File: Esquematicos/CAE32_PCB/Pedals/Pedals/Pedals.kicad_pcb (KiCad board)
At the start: 4 copper layers, 45 x 55 mm, 64 parts, among them J1 PGRM and SPI, J10 Conn_01x03_Female, J11 Conn_01x03_Female, J12 Conn_01x03_Female, J13 Conn_01x03_Female, J14 USB_C_Receptacle, J15 UART_PGR, J16 ST-Link, J2 Conn_01x07_Female, J3 Conn_01x03_Female, J4 Conn_01x03_Female, J5 Conn_01x03_Female, J6 Conn_01x03_Female, J7 Conn_01x03_Female, J8 Conn_01x03_Female, J9 Conn_01x03_Female, Q1 MMBT3906, SW1 BOOT, SW2 MODE, SW3 RST, U1 STM32F072RBTx, U2 REF3033, U3 ADC128S102, U4 HX711, U5 LDL1117

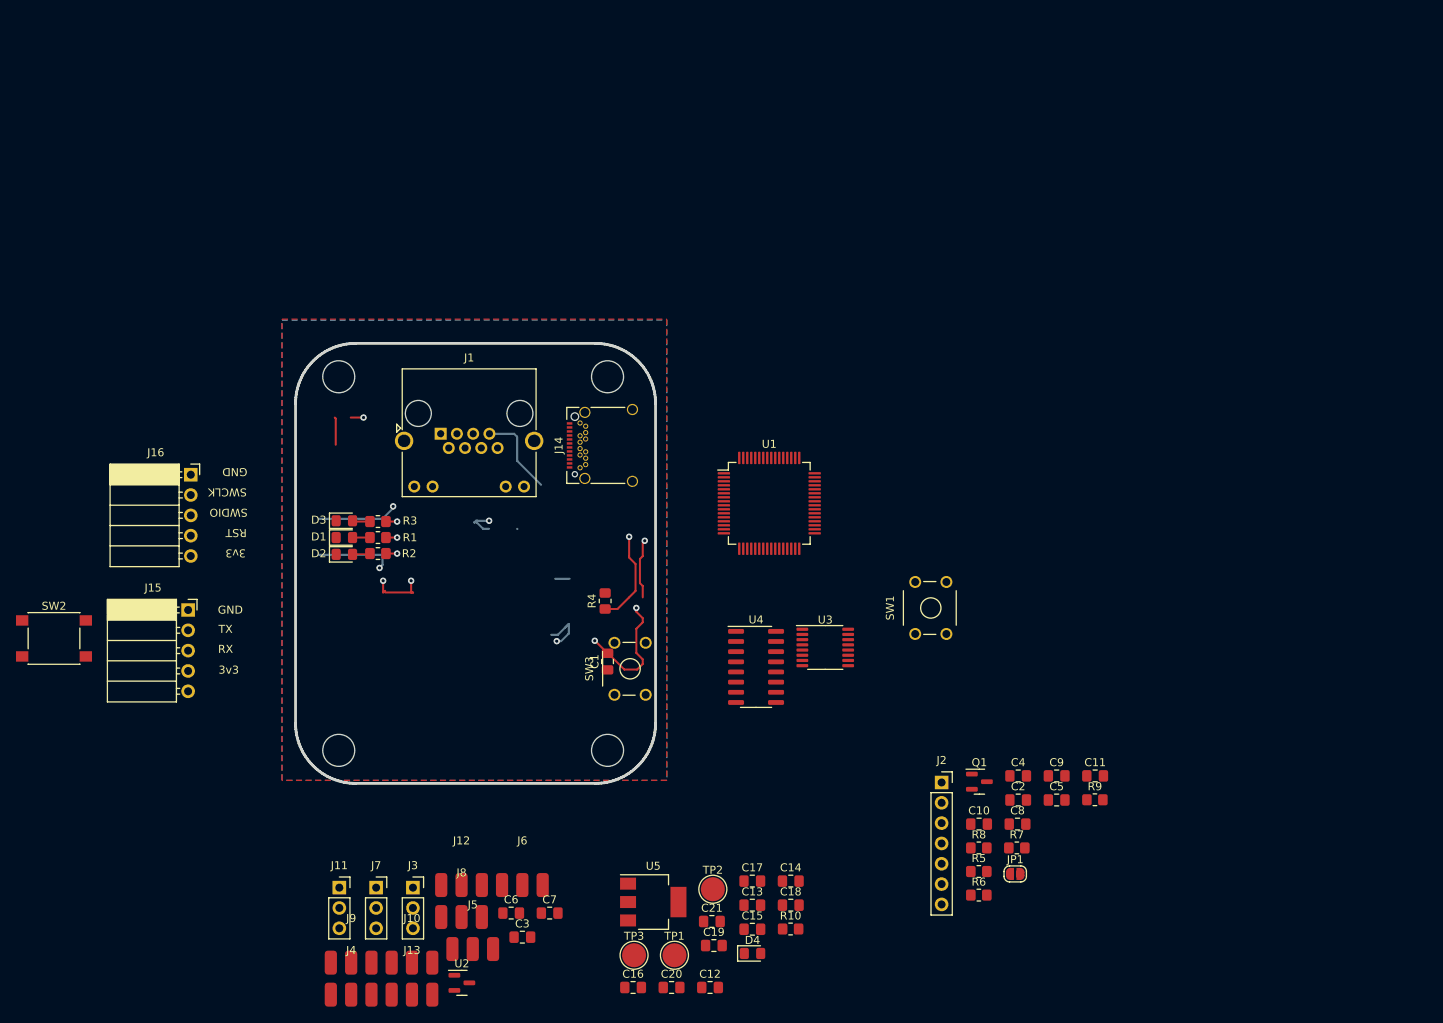
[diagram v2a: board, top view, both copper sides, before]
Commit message: update: se añade otra hoja para las celdas de carga, ademas de reorganizar todas las hojas
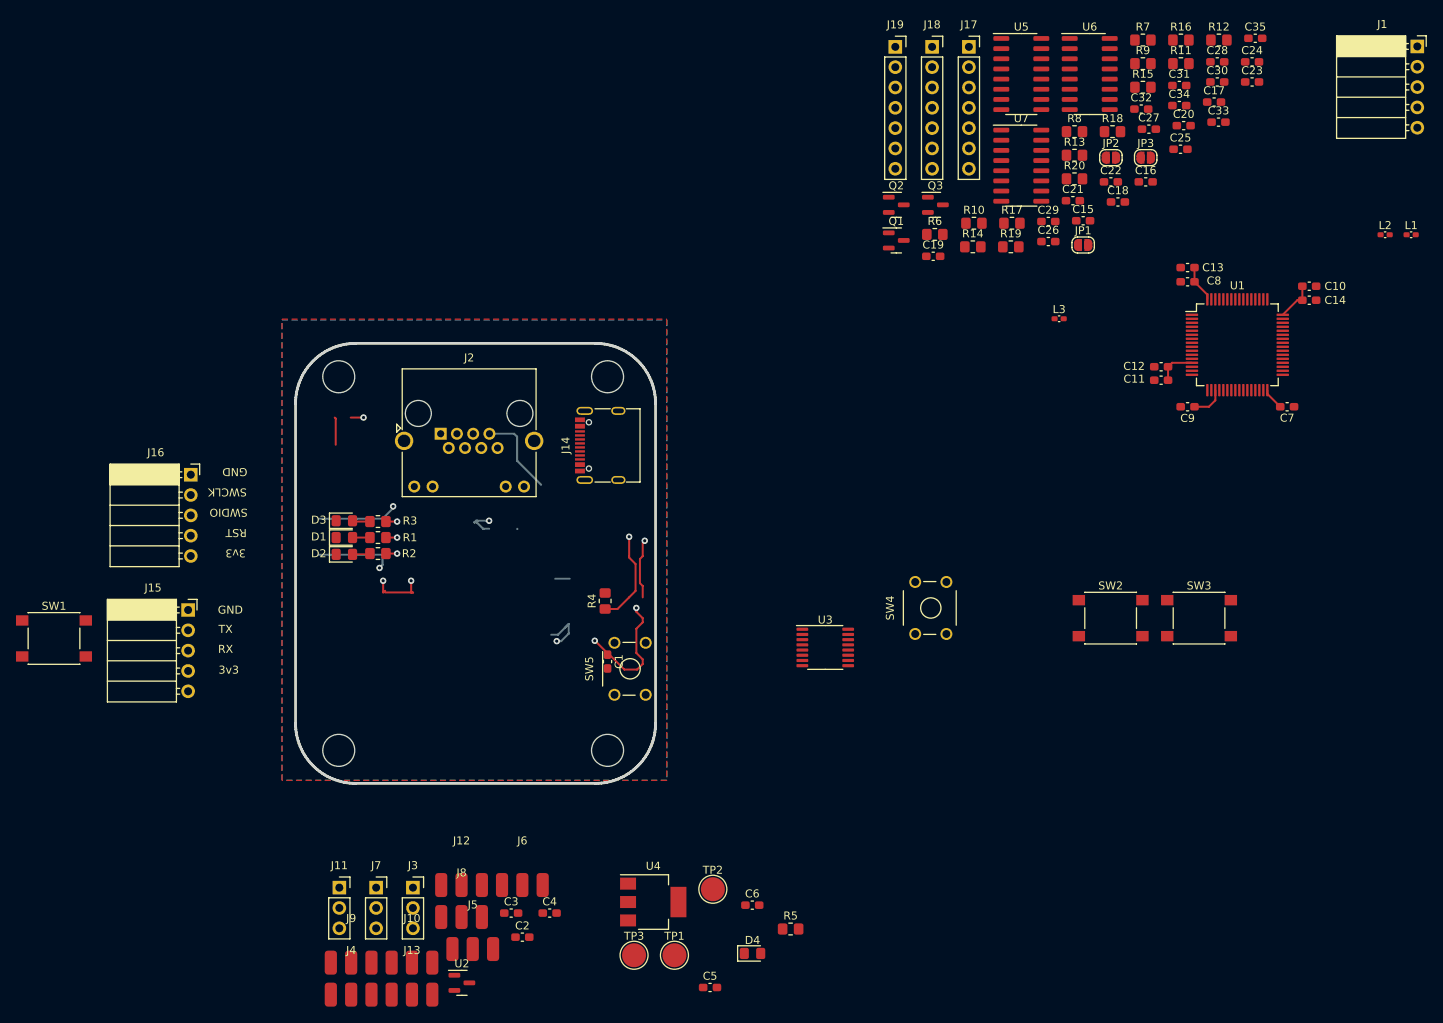
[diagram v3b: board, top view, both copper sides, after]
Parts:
- removed the C10 at (209.7, 131.9)
- removed the C11 at (224.2, 125.9)
- removed the C2 at (214.6, 128.9)
- removed the C4 at (214.6, 125.9)
- removed the C5 at (219.4, 128.9)
- removed the C8 at (214.6, 131.9)
- removed the C9 at (219.4, 125.9)
- removed the J2 at (205.1, 126.7)
- removed the R5 at (209.7, 137.8)
- removed the U4 at (181.9, 112.3)
- added C15: 0u1, Capacitor_SMD:C_0603_1608Metric_Pad1.08x0.95mm_HandSolder, F.Cu at (222.8, 56.5)
- added C16: 0u1, Capacitor_SMD:C_0603_1608Metric_Pad1.08x0.95mm_HandSolder, F.Cu at (230.6, 51.6)
- added C17: 0u1, Capacitor_SMD:C_0603_1608Metric_Pad1.08x0.95mm_HandSolder, F.Cu at (239.1, 41.7)
- added C18: 0u1, Capacitor_SMD:C_0603_1608Metric_Pad1.08x0.95mm_HandSolder, F.Cu at (227.1, 54.1)
- added C19: 10u, Capacitor_SMD:C_0603_1608Metric_Pad1.08x0.95mm_HandSolder, F.Cu at (204.0, 60.9)
- added C20: 10u, Capacitor_SMD:C_0603_1608Metric_Pad1.08x0.95mm_HandSolder, F.Cu at (235.3, 44.6)
- added C21: 0u1, Capacitor_SMD:C_0603_1608Metric_Pad1.08x0.95mm_HandSolder, F.Cu at (221.5, 54.0)
- added C22: 0u1, Capacitor_SMD:C_0603_1608Metric_Pad1.08x0.95mm_HandSolder, F.Cu at (226.2, 51.6)
- added C23: 0u1, Capacitor_SMD:C_0603_1608Metric_Pad1.08x0.95mm_HandSolder, F.Cu at (243.9, 39.1)
- added C24: 0u1, Capacitor_SMD:C_0603_1608Metric_Pad1.08x0.95mm_HandSolder, F.Cu at (243.9, 36.6)
- added C25: 0u1, Capacitor_SMD:C_0603_1608Metric_Pad1.08x0.95mm_HandSolder, F.Cu at (234.9, 47.6)
- added C26: 0u1, Capacitor_SMD:C_0603_1608Metric_Pad1.08x0.95mm_HandSolder, F.Cu at (218.4, 59.1)
- added C27: 10u, Capacitor_SMD:C_0603_1608Metric_Pad1.08x0.95mm_HandSolder, F.Cu at (231.0, 45.0)
- added C28: 10u, Capacitor_SMD:C_0603_1608Metric_Pad1.08x0.95mm_HandSolder, F.Cu at (239.5, 36.6)
- added C29: 0u1, Capacitor_SMD:C_0603_1608Metric_Pad1.08x0.95mm_HandSolder, F.Cu at (218.4, 56.6)
- added C30: 0u1, Capacitor_SMD:C_0603_1608Metric_Pad1.08x0.95mm_HandSolder, F.Cu at (239.5, 39.1)
- added C31: 10u, Capacitor_SMD:C_0603_1608Metric_Pad1.08x0.95mm_HandSolder, F.Cu at (234.8, 39.6)
- added C32: 0u1, Capacitor_SMD:C_0603_1608Metric_Pad1.08x0.95mm_HandSolder, F.Cu at (230.0, 42.5)
- added C33: 0u1, Capacitor_SMD:C_0603_1608Metric_Pad1.08x0.95mm_HandSolder, F.Cu at (239.7, 44.2)
- added C34: 0u1, Capacitor_SMD:C_0603_1608Metric_Pad1.08x0.95mm_HandSolder, F.Cu at (234.8, 42.1)
- added C35: 10u, Capacitor_SMD:C_0603_1608Metric_Pad1.08x0.95mm_HandSolder, F.Cu at (244.3, 33.7)
- added J1: SPI_MASTER, Connector_PinSocket_2.54mm:PinSocket_1x05_P2.54mm_Horizontal, F.Cu at (264.5, 34.7)
- added J17: Conn_01x07_Female, Connector_PinSocket_2.54mm:PinSocket_1x07_P2.54mm_Vertical, F.Cu at (208.5, 34.8)
- added J18: Conn_01x07_Female, Connector_PinSocket_2.54mm:PinSocket_1x07_P2.54mm_Vertical, F.Cu at (203.9, 34.8)
- added J19: Conn_01x07_Female, Connector_PinSocket_2.54mm:PinSocket_1x07_P2.54mm_Vertical, F.Cu at (199.3, 34.8)
- added JP2: SolderJumper_2_Open, Jumper:SolderJumper-2_P1.3mm_Open_RoundedPad1.0x1.5mm, F.Cu at (226.2, 48.6)
- added JP3: SolderJumper_2_Open, Jumper:SolderJumper-2_P1.3mm_Open_RoundedPad1.0x1.5mm, F.Cu at (230.6, 48.6)
- added L1: 3u3, Inductor_SMD:L_0402_1005Metric_Pad0.77x0.64mm_HandSolder, F.Cu at (263.8, 58.2)
- added L2: 3u3, Inductor_SMD:L_0402_1005Metric_Pad0.77x0.64mm_HandSolder, F.Cu at (260.5, 58.2)
- added L3: 3u3, Inductor_SMD:L_0402_1005Metric_Pad0.77x0.64mm_HandSolder, F.Cu at (219.8, 68.8)
- added Q2: MMBT3906, Package_TO_SOT_SMD:SOT-23, F.Cu at (199.4, 54.5)
- added Q3: MMBT3906, Package_TO_SOT_SMD:SOT-23, F.Cu at (204.3, 54.5)
- added R10: 20k, Resistor_SMD:R_0805_2012Metric_Pad1.20x1.40mm_HandSolder, F.Cu at (209.1, 56.8)
- added R11: 8.2k, Resistor_SMD:R_0805_2012Metric_Pad1.20x1.40mm_HandSolder, F.Cu at (235.0, 36.9)
- added R12: 20k, Resistor_SMD:R_0805_2012Metric_Pad1.20x1.40mm_HandSolder, F.Cu at (239.7, 33.9)
- added R13: 8.2k, Resistor_SMD:R_0805_2012Metric_Pad1.20x1.40mm_HandSolder, F.Cu at (221.7, 48.3)
- added R14: 10k, Resistor_SMD:R_0805_2012Metric_Pad1.20x1.40mm_HandSolder, F.Cu at (209.0, 59.8)
- added R15: 10k, Resistor_SMD:R_0805_2012Metric_Pad1.20x1.40mm_HandSolder, F.Cu at (230.2, 39.8)
- added R16: 100, Resistor_SMD:R_0805_2012Metric_Pad1.20x1.40mm_HandSolder, F.Cu at (235.0, 33.9)
- added R17: 100, Resistor_SMD:R_0805_2012Metric_Pad1.20x1.40mm_HandSolder, F.Cu at (213.8, 56.8)
- added R18: 20k, Resistor_SMD:R_0805_2012Metric_Pad1.20x1.40mm_HandSolder, F.Cu at (226.4, 45.4)
- added R19: 8.2k, Resistor_SMD:R_0805_2012Metric_Pad1.20x1.40mm_HandSolder, F.Cu at (213.7, 59.8)
- added R20: 10k, Resistor_SMD:R_0805_2012Metric_Pad1.20x1.40mm_HandSolder, F.Cu at (221.7, 51.3)
- added SW2: B2, Button_Switch_SMD:SW_Push_1P1T_NO_6x6mm_H9.5mm, F.Cu at (226.2, 106.2)
- added SW3: B3, Button_Switch_SMD:SW_Push_1P1T_NO_6x6mm_H9.5mm, F.Cu at (237.2, 106.2)
- added U5: HX711, Package_SO:SOP-16_3.9x9.9mm_P1.27mm, F.Cu at (215.0, 38.2)
- added U6: HX711, Package_SO:SOP-16_3.9x9.9mm_P1.27mm, F.Cu at (223.6, 38.2)
- added U7: HX711, Package_SO:SOP-16_3.9x9.9mm_P1.27mm, F.Cu at (215.0, 49.6)
- C1: footprint Capacitor_SMD:C_0805_2012Metric_Pad1.18x1.45mm_HandSolder -> Capacitor_SMD:C_0603_1608Metric_Pad1.08x0.95mm_HandSolder
- C10: renamed from C17; footprint Capacitor_SMD:C_0805_2012Metric_Pad1.18x1.45mm_HandSolder -> Capacitor_SMD:C_0603_1608Metric_Pad1.08x0.95mm_HandSolder
- C11: renamed from C18; footprint Capacitor_SMD:C_0805_2012Metric_Pad1.18x1.45mm_HandSolder -> Capacitor_SMD:C_0603_1608Metric_Pad1.08x0.95mm_HandSolder
- C12: renamed from C19; footprint Capacitor_SMD:C_0805_2012Metric_Pad1.18x1.45mm_HandSolder -> Capacitor_SMD:C_0603_1608Metric_Pad1.08x0.95mm_HandSolder
- C13: renamed from C20; footprint Capacitor_SMD:C_0805_2012Metric_Pad1.18x1.45mm_HandSolder -> Capacitor_SMD:C_0603_1608Metric_Pad1.08x0.95mm_HandSolder
- C14: renamed from C21; footprint Capacitor_SMD:C_0805_2012Metric_Pad1.18x1.45mm_HandSolder -> Capacitor_SMD:C_0603_1608Metric_Pad1.08x0.95mm_HandSolder
- C2: renamed from C3; footprint Capacitor_SMD:C_0805_2012Metric_Pad1.18x1.45mm_HandSolder -> Capacitor_SMD:C_0603_1608Metric_Pad1.08x0.95mm_HandSolder
- C3: renamed from C6; footprint Capacitor_SMD:C_0805_2012Metric_Pad1.18x1.45mm_HandSolder -> Capacitor_SMD:C_0603_1608Metric_Pad1.08x0.95mm_HandSolder
- C4: renamed from C7; footprint Capacitor_SMD:C_0805_2012Metric_Pad1.18x1.45mm_HandSolder -> Capacitor_SMD:C_0603_1608Metric_Pad1.08x0.95mm_HandSolder
- C5: renamed from C12; footprint Capacitor_SMD:C_0805_2012Metric_Pad1.18x1.45mm_HandSolder -> Capacitor_SMD:C_0603_1608Metric_Pad1.08x0.95mm_HandSolder
- C6: renamed from C13; footprint Capacitor_SMD:C_0805_2012Metric_Pad1.18x1.45mm_HandSolder -> Capacitor_SMD:C_0603_1608Metric_Pad1.08x0.95mm_HandSolder
- C7: renamed from C14; footprint Capacitor_SMD:C_0805_2012Metric_Pad1.18x1.45mm_HandSolder -> Capacitor_SMD:C_0603_1608Metric_Pad1.08x0.95mm_HandSolder
- C8: renamed from C15; footprint Capacitor_SMD:C_0805_2012Metric_Pad1.18x1.45mm_HandSolder -> Capacitor_SMD:C_0603_1608Metric_Pad1.08x0.95mm_HandSolder
- C9: renamed from C16; footprint Capacitor_SMD:C_0805_2012Metric_Pad1.18x1.45mm_HandSolder -> Capacitor_SMD:C_0603_1608Metric_Pad1.08x0.95mm_HandSolder
- J14: footprint Connector_USB:USB_C_Receptacle_Amphenol_12401548E4-2A_CircularHoles -> Connector_USB:USB_C_Receptacle_G-Switch_GT-USB-7010ASV
- R7: value 20k -> 100
- R8: value 8.2k -> 100
- R9: value 10k -> 100
- SW1: renamed from SW2; value MODE -> B1
- moved C13 110.7 mm to (235.8, 62.4), turned to 180 degrees
- moved C14 107.7 mm to (251.0, 66.4)
- moved R7 102.2 mm to (230.2, 33.9)
- moved C10 101.9 mm to (251.0, 64.7)
- moved C9 100.4 mm to (235.8, 79.8), turned to 180 degrees
- moved C8 97.5 mm to (235.8, 64.1), turned to 180 degrees
- moved R9 92.2 mm to (230.2, 36.9)
- moved C12 91.4 mm to (232.5, 74.8), turned to 180 degrees
- moved R8 90.3 mm to (221.7, 45.4)
- moved C7 85.8 mm to (248.2, 79.8)
- moved R6 82.8 mm to (204.2, 58.2)
- moved C11 80.3 mm to (232.5, 76.4), turned to 180 degrees
- moved JP1 79.1 mm to (222.8, 59.5)
- moved Q1 68.4 mm to (199.4, 59.0)
- moved U1 61.8 mm to (242.0, 72.0)
- renumbered J1 to J2, R10 to R5, SW1 to SW4, SW3 to SW5, U5 to U4
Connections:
- J14 pad A6: /Connectors(USB,Programming and debugging)/D+ -> /D+
- J14 pad A7: /Connectors(USB,Programming and debugging)/D- -> /D-
- J14 pad B6: /Connectors(USB,Programming and debugging)/D+ -> /D+
- J14 pad B7: /Connectors(USB,Programming and debugging)/D- -> /D-
- J15 pad 2: /Connectors(USB,Programming and debugging)/USART_TX -> /PGR_UART_TX
- J15 pad 3: /Connectors(USB,Programming and debugging)/USART_RX -> /PGR_UART_RX
- J2 pad 2: /MOSI -> unconnected-(J2-Pad2)
- J2 pad 4: /MISO -> /S_DOUT
- J2 pad 5: unconnected-(J1-Pad5) -> /S_DIN
- J2 pad 6: /CS_PDL -> /S_CS_PEDALS
- J2 pad 8: /SCKL -> /S_CKL
- JP1 pad 2: Net-(U4-Pad15) -> Net-(JP1-Pad2)
- Q1 pad 3: Net-(U4-Pad3) -> Net-(L1-Pad2)
- R1 pad 1: /IND0 -> /IND3
- R6 pad 1: Net-(U4-Pad7) -> /Load Cells/A2+
- R6 pad 2: /ADCs components/A- -> Net-(C17-Pad1)
- R7 pad 1: Net-(U4-Pad3) -> Net-(C17-Pad2)
- R7 pad 2: Net-(U4-Pad4) -> /Load Cells/A2-
- R8 pad 1: Net-(U4-Pad4) -> /Load Cells/A1+
- R8 pad 2: GNDREF -> Net-(C18-Pad1)
- R9 pad 1: Net-(U4-Pad15) -> Net-(C18-Pad2)
- R9 pad 2: +3.3V -> /Load Cells/A1-
- SW1 pad 1: /MODE -> /B1
- U1 pad 10: unconnected-(U1-Pad10) -> /IND3
- U1 pad 11: unconnected-(U1-Pad11) -> /S_DIN
- U1 pad 13: unconnected-(U1-Pad13) -> +3.3V
- U1 pad 14: unconnected-(U1-Pad14) -> /LOAD_CELL_CLK
- U1 pad 19: unconnected-(U1-Pad19) -> +3.3V
- U1 pad 20: unconnected-(U1-Pad20) -> /CS_ADC
- U1 pad 21: unconnected-(U1-Pad21) -> /SCKL
- U1 pad 22: unconnected-(U1-Pad22) -> /DOUT
- U1 pad 23: unconnected-(U1-Pad23) -> /DIN
- U1 pad 24: unconnected-(U1-Pad24) -> /UART_RX
- U1 pad 25: unconnected-(U1-Pad25) -> /UART_TX
- U1 pad 26: unconnected-(U1-Pad26) -> /LOAD_CELL_3
- U1 pad 29: unconnected-(U1-Pad29) -> /S_CKL
- U1 pad 32: unconnected-(U1-Pad32) -> +3.3V
- U1 pad 33: unconnected-(U1-Pad33) -> /S_CS_PEDALS
- U1 pad 35: unconnected-(U1-Pad35) -> /S_DOUT
- U1 pad 37: unconnected-(U1-Pad37) -> /LOAD_CELL_2
- U1 pad 38: unconnected-(U1-Pad38) -> /LOAD_CELL_1
- U1 pad 39: unconnected-(U1-Pad39) -> /B3
- U1 pad 40: unconnected-(U1-Pad40) -> /B2
- U1 pad 41: unconnected-(U1-Pad41) -> /B1
- U1 pad 42: unconnected-(U1-Pad42) -> /PGR_UART_RX
- U1 pad 43: unconnected-(U1-Pad43) -> /PGR_UART_TX
- U1 pad 44: unconnected-(U1-Pad44) -> /D-
- U1 pad 45: unconnected-(U1-Pad45) -> /D+
- U1 pad 48: unconnected-(U1-Pad48) -> +3.3V
- U1 pad 61: unconnected-(U1-Pad61) -> /CAN_RX
- U1 pad 62: unconnected-(U1-Pad62) -> /CAN_TX
- U1 pad 64: unconnected-(U1-Pad64) -> +3.3V
- U1 pad 8: unconnected-(U1-Pad8) -> /IND1
- U1 pad 9: unconnected-(U1-Pad9) -> /IND2
- U3 pad 1: /ADCs components/CS -> /CS_ADC
- U3 pad 14: /ADCs components/DIN -> /DIN
- U3 pad 15: /ADCs components/DOUT -> /DOUT
- U3 pad 16: /ADCs components/SCLK -> /SCKL
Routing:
- net /S_DOUT: track 0.00 -> 26.8 mm
- net /MISO: track 26.8 -> 0.00 mm
- net /S_CKL: track 0.00 -> 23.4 mm
- net /SCKL: track 23.4 -> 0.00 mm
- net +3.3V: track 15.9 -> 37.4 mm
- net unconnected-(J2-Pad2): track 0.00 -> 14.9 mm
- net /MOSI: track 14.9 -> 0.00 mm
- net /MODE: track 13.3 -> 0.00 mm, vias 1 -> 0
- net (no net): track 19.2 -> 32.5 mm
- net /S_CS_PEDALS: track 0.00 -> 8.18 mm
- net /CS_PDL: track 8.18 -> 0.00 mm
- net /IND3: track 0.00 -> 1.40 mm, vias 0 -> 1
- net /IND0: track 1.40 -> 0.00 mm, vias 1 -> 0
- net /B1: vias 0 -> 1

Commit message: update: Componentes acomodados en la PCB
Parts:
- removed the SW2 at (226.2, 106.2)
- removed the SW3 at (237.2, 106.2)
- added H1: M, MountingHole:MountingHole_3.2mm_M3_Pad_Via, F.Cu at (190.0, 127.4)
- added H2: M, MountingHole:MountingHole_3.2mm_M3_Pad_Via, F.Cu at (106.7, 127.7)
- added H3: M, MountingHole:MountingHole_3.2mm_M3_Pad_Via, F.Cu at (106.6, 62.1)
- added H4: M, MountingHole:MountingHole_3.2mm_M3_Pad_Via, F.Cu at (190.0, 62.1)
- added J2: Conn_01x02_Male, Connector_PinHeader_2.54mm:PinHeader_1x02_P2.54mm_Vertical, F.Cu at (156.0, 67.3)
- J10: renamed from J9; moved to B.Cu
- J11: renamed from J10; moved to B.Cu
- J14: renamed from J13; moved to B.Cu
- J18: renamed from J17; value Conn_01x07_Female -> LC_2
- J19: renamed from J18; value Conn_01x07_Female -> LD_1
- J20: renamed from J19; value Conn_01x07_Female -> LC_3
- J6: renamed from J5; moved to B.Cu
- J7: renamed from J6; moved to B.Cu
- R1, R10, R11, R12, R13, R14, R15, R16, R17, R18, R19, R2, R20, R3, R4, R5, R6, R7, R8, R9: footprint Resistor_SMD:R_0805_2012Metric_Pad1.20x1.40mm_HandSolder -> Resistor_SMD:R_0603_1608Metric_Pad0.98x0.95mm_HandSolder
- SW1: value B1 -> CONFIG; footprint Button_Switch_SMD:SW_Push_1P1T_NO_6x6mm_H9.5mm -> Button_Switch_SMD:SW_DIP_SPSTx03_Slide_6.7x9.18mm_W6.73mm_P2.54mm_LowProfile_JPin
- moved L1 137.8 mm to (138.9, 116.5), turned to 90 degrees
- moved C16 125.3 mm to (134.6, 98.0)
- moved R7 125.0 mm to (140.1, 120.5), turned to -90 degrees
- moved C21 122.4 mm to (134.6, 99.7)
- moved R11 122.4 mm to (141.6, 115.9)
- moved C23 120.5 mm to (145.3, 117.3), turned to 180 degrees
- moved J18 119.2 mm to (132.9, 126.9), turned to 90 degrees
- moved R16 116.6 mm to (156.9, 120.5), turned to 90 degrees
- moved C34 116.1 mm to (149.9, 118.7), turned to 180 degrees
- moved C15 113.1 mm to (147.3, 98.0), turned to 180 degrees
- moved L2 113.0 mm to (163.7, 116.5), turned to 90 degrees
- moved C33 112.0 mm to (159.2, 117.3), turned to 180 degrees
- moved C32 108.1 mm to (159.9, 101.4)
- moved R12 107.9 mm to (165.9, 112.5)
- moved C19 107.4 mm to (136.5, 120.5), turned to 180 degrees
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- renumbered C23 to C15, C24 to C16, C25 to C17, C26 to C18, C15 to C19, C27 to C20, C28 to C21, C16 to C22, C17 to C23, C18 to C24, C19 to C25, C20 to C26, C21 to C27, C22 to C28, C33 to C29, C34 to C30, C29 to C31, C35 to C32, C30 to C33, C31 to C34, C32 to C35, J11 to J12, J12 to J13, J14 to J15, J15 to J16, J16 to J17, J2 to J3, J3 to J4, J4 to J5, J7 to J8, J8 to J9, SW4 to SW2, SW5 to SW3
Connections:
- J16 pad 2: /PGR_UART_TX -> /PGR_UART_RX
- J16 pad 3: /PGR_UART_RX -> /PGR_UART_TX
- J20 pad 2: /Load Cells/B2+ -> /Load Cells/B3+
- SW1 pad 1: /B1 -> GNDREF
- U1 pad 12: unconnected-(U1-Pad12) -> GNDREF
- U1 pad 18: unconnected-(U1-Pad18) -> GNDREF
- U1 pad 31: unconnected-(U1-Pad31) -> GNDREF
- U1 pad 47: unconnected-(U1-Pad47) -> GNDREF
- U1 pad 63: unconnected-(U1-Pad63) -> GNDREF
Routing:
- net /DOUT: track 0.00 -> 83.6 mm, vias 0 -> 2
- net /LOAD_CELL_CLK: track 0.00 -> 71.0 mm, vias 0 -> 4
- net /SCKL: track 0.00 -> 69.8 mm, vias 0 -> 2
- net /S_CS_PEDALS: track 8.18 -> 56.7 mm, vias 0 -> 1
- net /ADCs components/Custom_4: track 0.00 -> 46.0 mm, vias 0 -> 2
- net /S_CKL: track 23.4 -> 65.8 mm, vias 0 -> 1
- net /S_DIN: track 0.00 -> 42.1 mm, vias 0 -> 2
- net /CS_ADC: track 0.00 -> 38.6 mm, vias 0 -> 2
- net /DIN: track 0.00 -> 35.5 mm, vias 0 -> 2
- net /LOAD_CELL_2: track 0.00 -> 34.1 mm, vias 0 -> 2
- net (no net): track 32.5 -> 0.00 mm
- net /PGR_UART_RX: track 0.00 -> 31.8 mm, vias 0 -> 1
- net /PGR_UART_TX: track 0.00 -> 31.2 mm, vias 0 -> 1
- net /Load Cells/B2+: track 0.00 -> 29.6 mm, vias 0 -> 1
- net /BOOT: track 27.4 -> 56.6 mm
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- added copper zone on B.Cu, net GNDREF
- removed copper zone on B.Cu, net +3.3V
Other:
- board size 45 x 55 mm -> 94.9 x 76.5 mm
- board text removed: "5V"
- board text removed: "BOOT"
- board text removed: "CS"
- board text removed: "MISO"
- board text removed: "MOSI"
- board text removed: "SCKL"

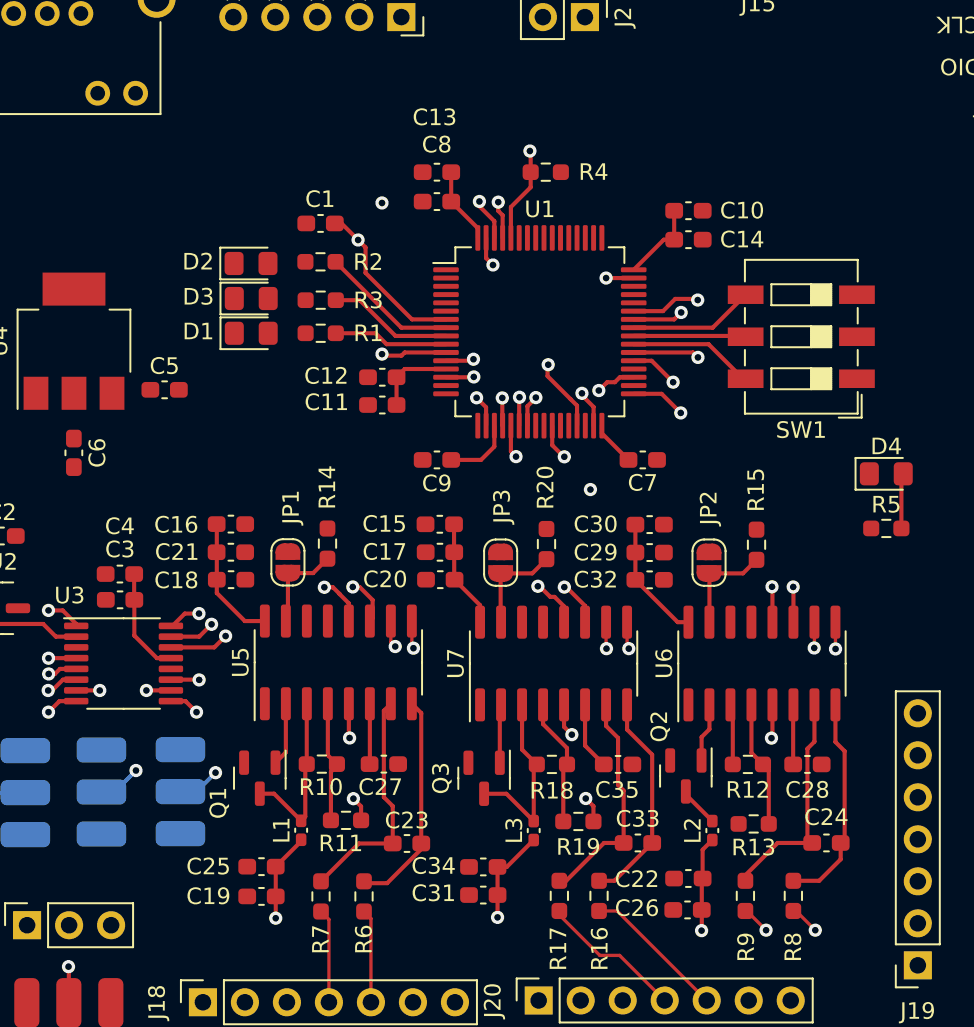
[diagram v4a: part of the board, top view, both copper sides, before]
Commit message: update: se agrega el consumo de corriente a los IC's ademas de agregar el URL y numero de parte de los componentes de LCSC en kicad
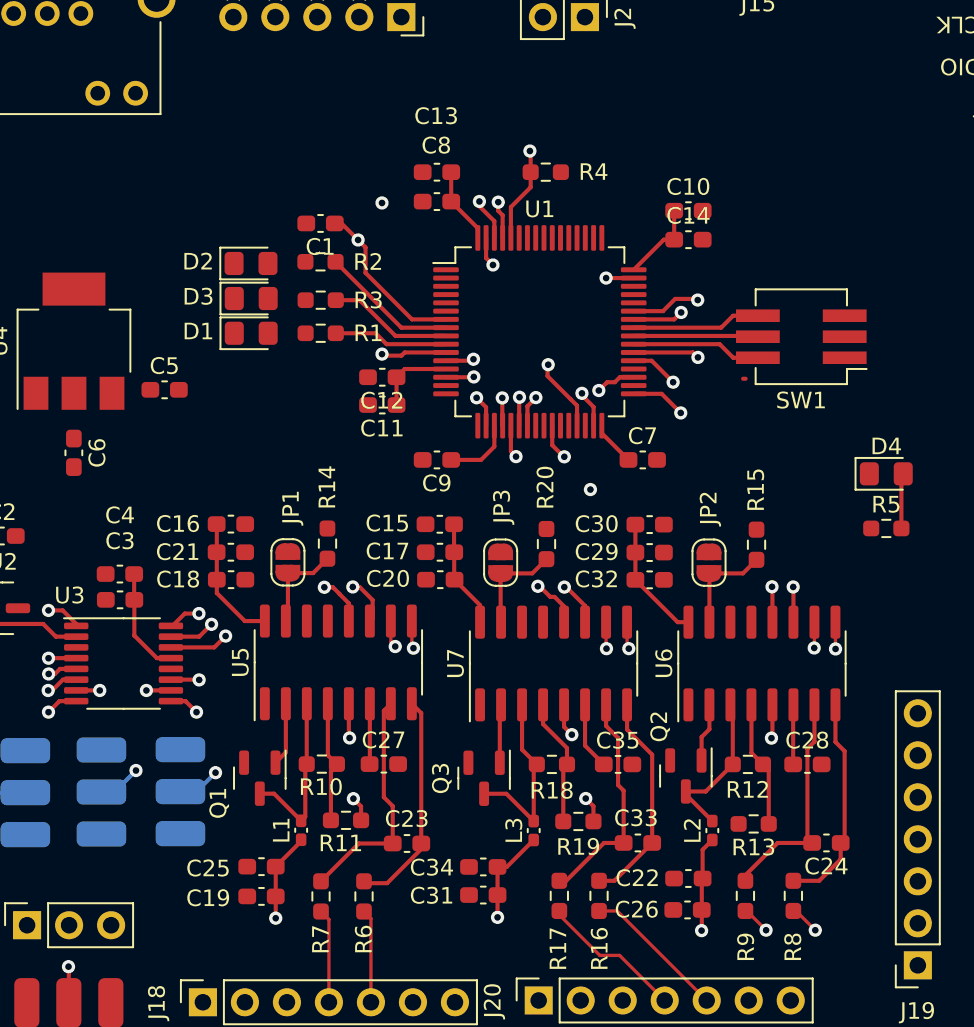
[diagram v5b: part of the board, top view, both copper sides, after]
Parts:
- C1: value 0.1uf -> 100n
- C15, C16, C17, C18, C19, C22, C23, C24, C27, C28, C29, C3, C30, C31, C33, C35, C4: value 0u1 -> 100n
- C5: value 1uf -> 1u
- C6: value 4.7uf -> 4u7
- D1: value LED_1 -> LED
- D2: value LED_2 -> LED
- D3: value LED_3 -> LED
- D4: value PWR -> LED
- J19: value LD_1 -> LC_1
- J2: value Conn_01x02_Male -> CAN
- R1, R2, R3: value 10 -> 330
- R5: value 43 -> 330
- SW1: footprint Button_Switch_SMD:SW_DIP_SPSTx03_Slide_6.7x9.18mm_W6.73mm_P2.54mm_LowProfile_JPin -> Button_Switch_SMD:SW_DIP_SPSTx03_Slide_KingTek_DSHP03TJ_W5.25mm_P1.27mm_JPin
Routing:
- net Net-(L2-Pad2): track 6.11 -> 9.63 mm
